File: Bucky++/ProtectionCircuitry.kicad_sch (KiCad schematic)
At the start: 0 parts

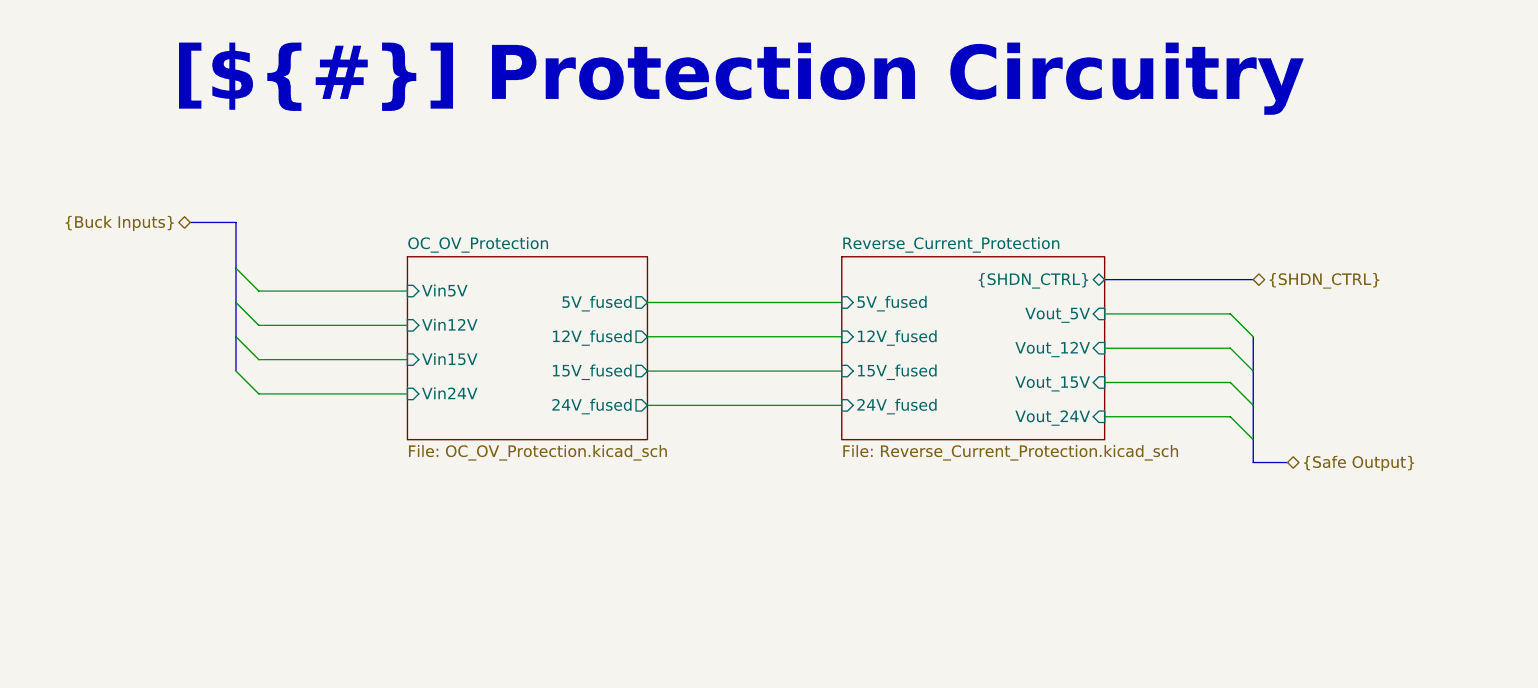
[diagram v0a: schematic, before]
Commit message: added over-current protection on main input
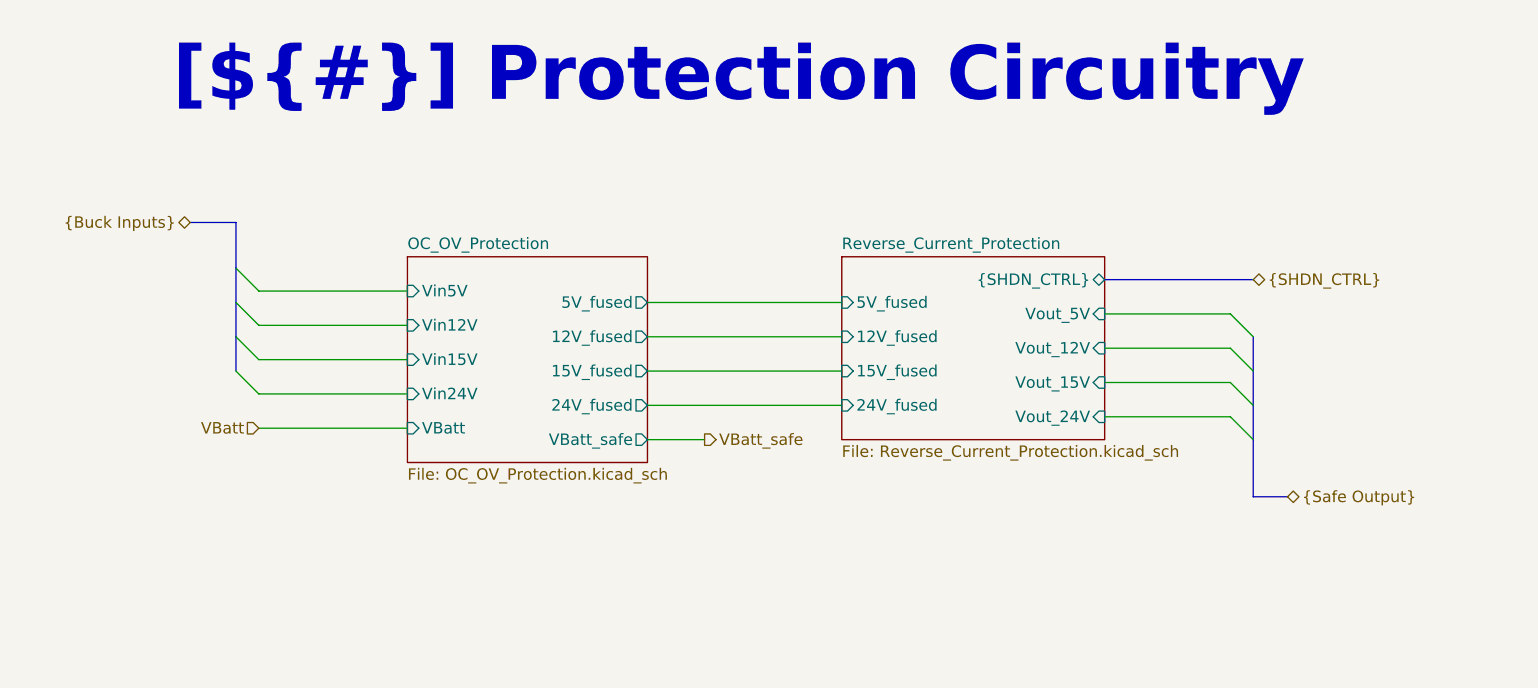
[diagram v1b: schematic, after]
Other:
- sheet OC_OV_Protection ports: added VBatt, VBatt_safe; removed none
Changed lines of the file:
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@@
+		)
+	)
+	(wire
+		(pts
+			(xy 144.78 59.69) (xy 158.75 59.69)
+		)
+		(stroke
+			(width 0)
+			(type default)
 		)
 	)
@@
 	(wire
 		(pts
+			(xy 50.8 60.96) (xy 67.31 60.96)
+		)
+		(stroke
+			(width 0)
+			(type default)
+		)
+	)
+	(wire
+		(pts
 			(xy 50.8 49.53) (xy 67.31 49.53)
 		)
@@
 	(bus
 		(pts
-			(xy 161.29 64.77) (xy 165.1 64.77)
+			(xy 161.29 68.58) (xy 165.1 68.58)
 		)
 		(stroke
@@
 	(wire
 		(pts
+			(xy 93.98 62.23) (xy 100.33 62.23)
+		)
+		(stroke
+			(width 0)
+			(type default)
+		)
+	)
+	(wire
+		(pts
 			(xy 93.98 58.42) (xy 115.57 58.42)
 		)
@@
 	(wire
 		(pts
-			(xy 144.78 59.69) (xy 158.75 59.69)
-		)
-		(stroke
-			(width 0)
-			(type default)
-		)
-	)
-	(wire
-		(pts
 			(xy 50.8 53.34) (xy 67.31 53.34)
 		)
@@
 	(bus
 		(pts
-			(xy 161.29 62.23) (xy 161.29 64.77)
+			(xy 161.29 62.23) (xy 161.29 68.58)
 		)
 		(stroke
@@
 	(hierarchical_label "{Safe Output}"
 		(shape tri_state)
-		(at 165.1 64.77 0)
+		(at 165.1 68.58 0)
 		(effects
 			(font
@@
 			)
 			(justify left)
+		)
+	)
+	(hierarchical_label "VBatt_safe"
+		(shape output)
+		(at 100.33 62.23 0)
+		(effects
+			(font
+				(size 1.27 1.27)
+			)
+			(justify left)
+		)
+	)
+	(hierarchical_label "VBatt"
+		(shape input)
+		(at 50.8 60.96 180)
+		(effects
+			(font
+				(size 1.27 1.27)
+			)
+			(justify right)
 		)
 	)
 	(sheet
 		(at 67.31 41.91)
-		(size 26.67 20.32)
+		(size 26.67 22.86)
 		(exclude_from_sim no)
 		(in_bom yes)
@@
 		)
 		(property "Sheetfile" "OC_OV_Protection.kicad_sch"
-			(at 67.31 62.8146 0)
+			(at 67.31 65.3546 0)
 			(effects
 				(font
@@
 			)
 		)
+		(pin "VBatt" input
+			(at 67.31 60.96 180)
+			(effects
+				(font
+					(size 1.27 1.27)
+				)
+				(justify left)
+			)
+		)
+		(pin "VBatt_safe" output
+			(at 93.98 62.23 0)
+			(effects
+				(font
+					(size 1.27 1.27)
+				)
+				(justify right)
+			)
+		)

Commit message: fixed errors and added protection diodes
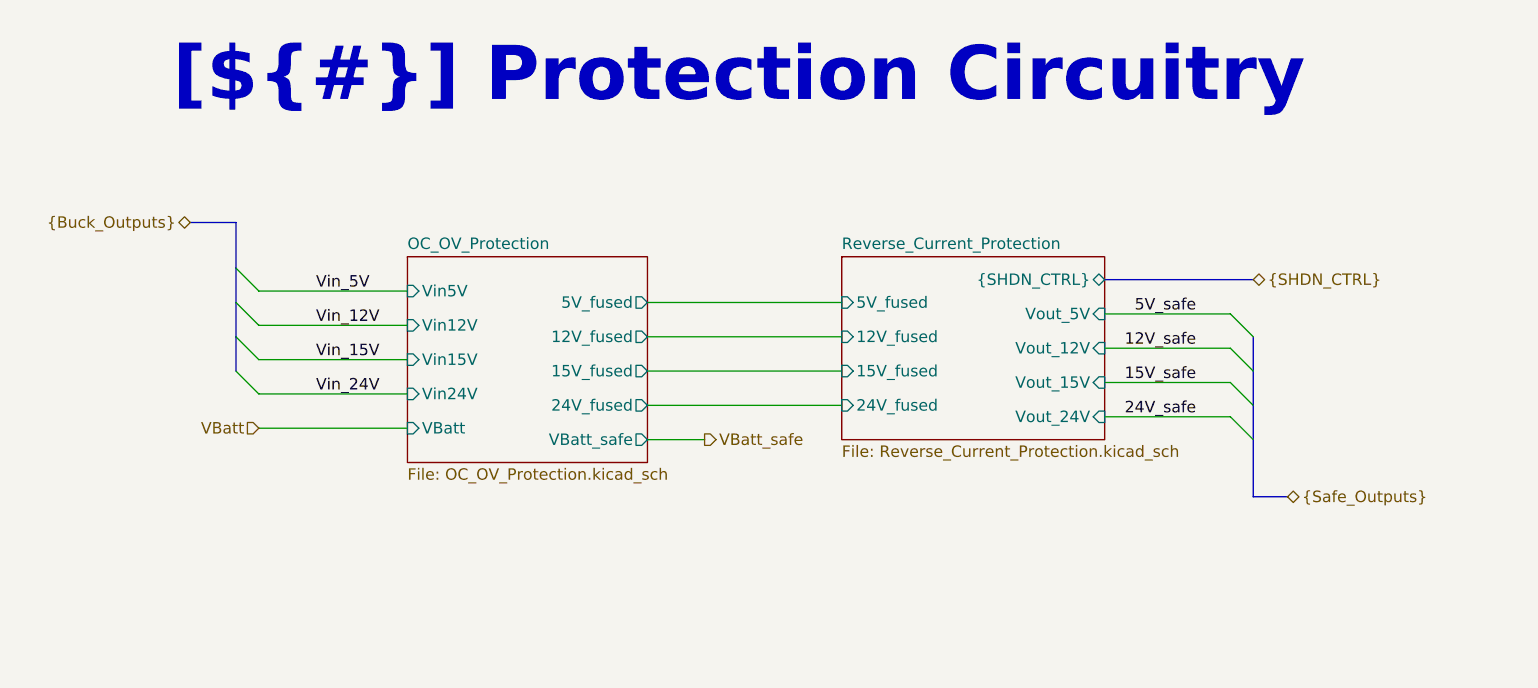
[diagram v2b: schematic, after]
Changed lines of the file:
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@@
+		)
+	)
+	(label "Vin_5V"
+		(at 57.15 45.72 0)
+		(effects
+			(font
+				(size 1.27 1.27)
+			)
+			(justify left bottom)
+		)
+	)
+	(label "Vin_15V"
+		(at 57.15 53.34 0)
+		(effects
+			(font
+				(size 1.27 1.27)
+			)
+			(justify left bottom)
+		)
+	)
+	(label "5V_safe"
+		(at 154.94 48.26 180)
+		(effects
+			(font
+				(size 1.27 1.27)
+			)
+			(justify right bottom)
+		)
+	)
+	(label "24V_safe"
+		(at 154.94 59.69 180)
+		(effects
+			(font
+				(size 1.27 1.27)
+			)
+			(justify right bottom)
+		)
+	)
+	(label "Vin_24V"
+		(at 57.15 57.15 0)
+		(effects
+			(font
+				(size 1.27 1.27)
+			)
+			(justify left bottom)
+		)
+	)
+	(label "Vin_12V"
+		(at 57.15 49.53 0)
+		(effects
+			(font
+				(size 1.27 1.27)
+			)
+			(justify left bottom)
+		)
+	)
+	(label "12V_safe"
+		(at 154.94 52.07 180)
+		(effects
+			(font
+				(size 1.27 1.27)
+			)
+			(justify right bottom)
+		)
+	)
+	(label "15V_safe"
+		(at 154.94 55.88 180)
+		(effects
+			(font
+				(size 1.27 1.27)
+			)
+			(justify right bottom)
 		)
 	)
@@
 		)
 	)
-	(hierarchical_label "{Buck Inputs}"
+	(hierarchical_label "{Buck_Outputs}"
 		(shape tri_state)
 		(at 43.18 38.1 180)
@@
 		)
 	)
-	(hierarchical_label "{Safe Output}"
+	(hierarchical_label "{Safe_Outputs}"
 		(shape tri_state)
 		(at 165.1 68.58 0)

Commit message: worked on layout, added adm1270
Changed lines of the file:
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@@
-	)
-	(bus_entry
-		(at 48.26 43.18)
-		(size 2.54 2.54)
-		(stroke
-			(width 0)
-			(type default)
-		)
 	)
 	(bus_entry
@@
 	)
 	(bus_entry
-		(at 48.26 50.8)
-		(size 2.54 2.54)
-		(stroke
-			(width 0)
-			(type default)
-		)
-	)
-	(bus_entry
-		(at 48.26 46.99)
+		(at 53.34 43.18)
 		(size 2.54 2.54)
 		(stroke
@@
 	)
 	(bus_entry
-		(at 48.26 54.61)
-		(size 2.54 2.54)
-		(stroke
-			(width 0)
-			(type default)
-		)
-	)
-	(wire
-		(pts
-			(xy 50.8 57.15) (xy 67.31 57.15)
-		)
+		(at 53.34 54.61)
+		(size 2.54 2.54)
+		(stroke
+			(width 0)
+			(type default)
+		)
+	)
+	(bus_entry
+		(at 53.34 46.99)
+		(size 2.54 2.54)
+		(stroke
+			(width 0)
+			(type default)
+		)
+	)
+	(bus_entry
+		(at 53.34 50.8)
+		(size 2.54 2.54)
 		(stroke
 			(width 0)
@@
 		)
 	)
-	(bus
-		(pts
-			(xy 48.26 46.99) (xy 48.26 50.8)
-		)
-		(stroke
-			(width 0)
-			(type default)
-		)
-	)
 	(wire
 		(pts
@@
 		)
 	)
-	(bus
-		(pts
-			(xy 48.26 43.18) (xy 48.26 46.99)
+	(wire
+		(pts
+			(xy 176.53 52.07) (xy 179.07 52.07)
 		)
 		(stroke
@@
 	(wire
 		(pts
-			(xy 50.8 49.53) (xy 67.31 49.53)
+			(xy 55.88 45.72) (xy 67.31 45.72)
+		)
+		(stroke
+			(width 0)
+			(type default)
+		)
+	)
+	(bus
+		(pts
+			(xy 53.34 43.18) (xy 53.34 38.1)
 		)
 		(stroke
@@
 		)
 	)
+	(bus
+		(pts
+			(xy 53.34 54.61) (xy 53.34 50.8)
+		)
+		(stroke
+			(width 0)
+			(type default)
+		)
+	)
+	(wire
+		(pts
+			(xy 55.88 49.53) (xy 67.31 49.53)
+		)
+		(stroke
+			(width 0)
+			(type default)
+		)
+	)
 	(wire
 		(pts
@@
 		)
 	)
+	(bus
+		(pts
+			(xy 53.34 38.1) (xy 45.72 38.1)
+		)
+		(stroke
+			(width 0)
+			(type default)
+		)
+	)
 	(wire
 		(pts
@@
 	(bus
 		(pts
-			(xy 43.18 38.1) (xy 48.26 38.1)
-		)
-		(stroke
-			(width 0)
-			(type default)
-		)
-	)
-	(bus
-		(pts
-			(xy 48.26 50.8) (xy 48.26 54.61)
+			(xy 53.34 46.99) (xy 53.34 43.18)
 		)
 		(stroke
@@
 		)
 	)
+	(wire
+		(pts
+			(xy 55.88 53.34) (xy 67.31 53.34)
+		)
+		(stroke
+			(width 0)
+			(type default)
+		)
+	)
+	(wire
+		(pts
+			(xy 55.88 57.15) (xy 67.31 57.15)
+		)
+		(stroke
+			(width 0)
+			(type default)
+		)
+	)
 	(bus
 		(pts
@@
 	(bus
 		(pts
-			(xy 48.26 38.1) (xy 48.26 43.18)
-		)
-		(stroke
-			(width 0)
-			(type default)
-		)
-	)
-	(wire
-		(pts
-			(xy 50.8 53.34) (xy 67.31 53.34)
+			(xy 53.34 50.8) (xy 53.34 46.99)
 		)
 		(stroke
@@
 		)
 	)
-	(wire
-		(pts
-			(xy 50.8 45.72) (xy 67.31 45.72)
-		)
-		(stroke
-			(width 0)
-			(type default)
-		)
-	)
 	(bus
 		(pts
@@
 		)
 	)
-	(label "Vin_5V"
-		(at 57.15 45.72 0)
-		(effects
-			(font
-				(size 1.27 1.27)
-			)
-			(justify left bottom)
-		)
-	)
-	(label "Vin_15V"
-		(at 57.15 53.34 0)
-		(effects
-			(font
-				(size 1.27 1.27)
-			)
-			(justify left bottom)
+	(label "12V_safe"
+		(at 176.53 52.07 180)
+		(effects
+			(font
+				(size 1.27 1.27)
+			)
+			(justify right bottom)
 		)
 	)
@@
 		)
 	)
+	(label "out24V"
+		(at 67.31 57.15 180)
+		(effects
+			(font
+				(size 1.27 1.27)
+			)
+			(justify right bottom)
+		)
+	)
 	(label "24V_safe"
 		(at 154.94 59.69 180)
@@
 		)
 	)
-	(label "Vin_24V"
-		(at 57.15 57.15 0)
-		(effects
-			(font
-				(size 1.27 1.27)
-			)
-			(justify left bottom)
-		)
-	)
-	(label "Vin_12V"
-		(at 57.15 49.53 0)
-		(effects
-			(font
-				(size 1.27 1.27)
-			)
-			(justify left bottom)
-		)
-	)
 	(label "12V_safe"
 		(at 154.94 52.07 180)
@@
 		)
 	)
+	(label "out12V"
+		(at 67.31 49.53 180)
+		(effects
+			(font
+				(size 1.27 1.27)
+			)
+			(justify right bottom)
+		)
+	)
+	(label "out5V"
+		(at 67.31 45.72 180)
+		(effects
+			(font
+				(size 1.27 1.27)
+			)
+			(justify right bottom)
+		)
+	)
 	(label "15V_safe"
 		(at 154.94 55.88 180)
+		(effects
+			(font
+				(size 1.27 1.27)
+			)
+			(justify right bottom)
+		)
+	)
+	(label "out15V"
+		(at 67.31 53.34 180)
 		(effects
 			(font
@@
 		)
 	)
-	(hierarchical_label "{Buck_Outputs}"
+	(hierarchical_label "{Shunt_Outputs}"
 		(shape tri_state)
-		(at 43.18 38.1 180)
+		(at 45.72 38.1 180)
 		(effects
 			(font
@@
 		)
 	)
-	(hierarchical_label "VBatt"
+	(hierarchical_label "12V_fans"
+		(shape output)
+		(at 179.07 52.07 0)
+		(effects
+			(font
+				(size 1.27 1.27)
+			)
+			(justify left)
+		)
+	)
+	(hierarchical_label "VBatt_protection"
 		(shape input)
 		(at 50.8 60.96 180)

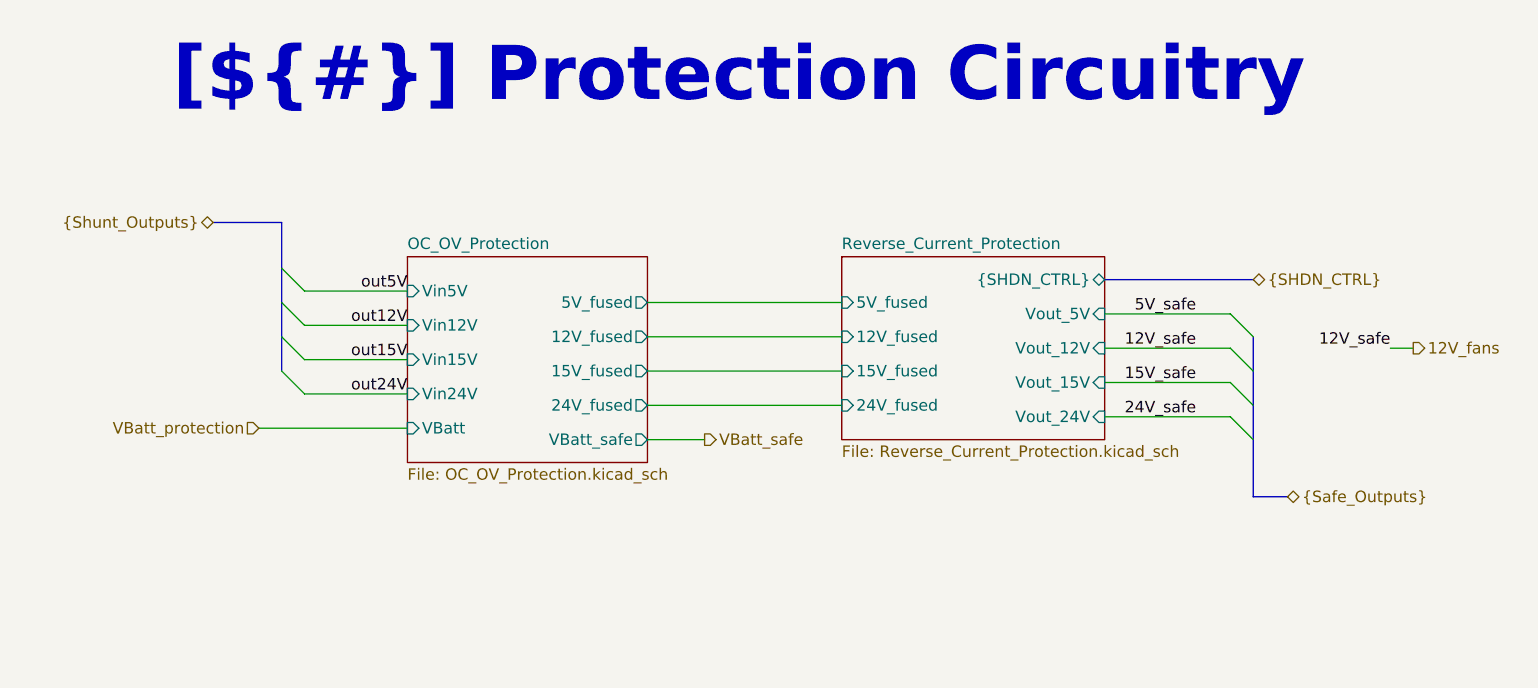
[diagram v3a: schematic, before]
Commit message: updated circuit after review. updated silkscreen
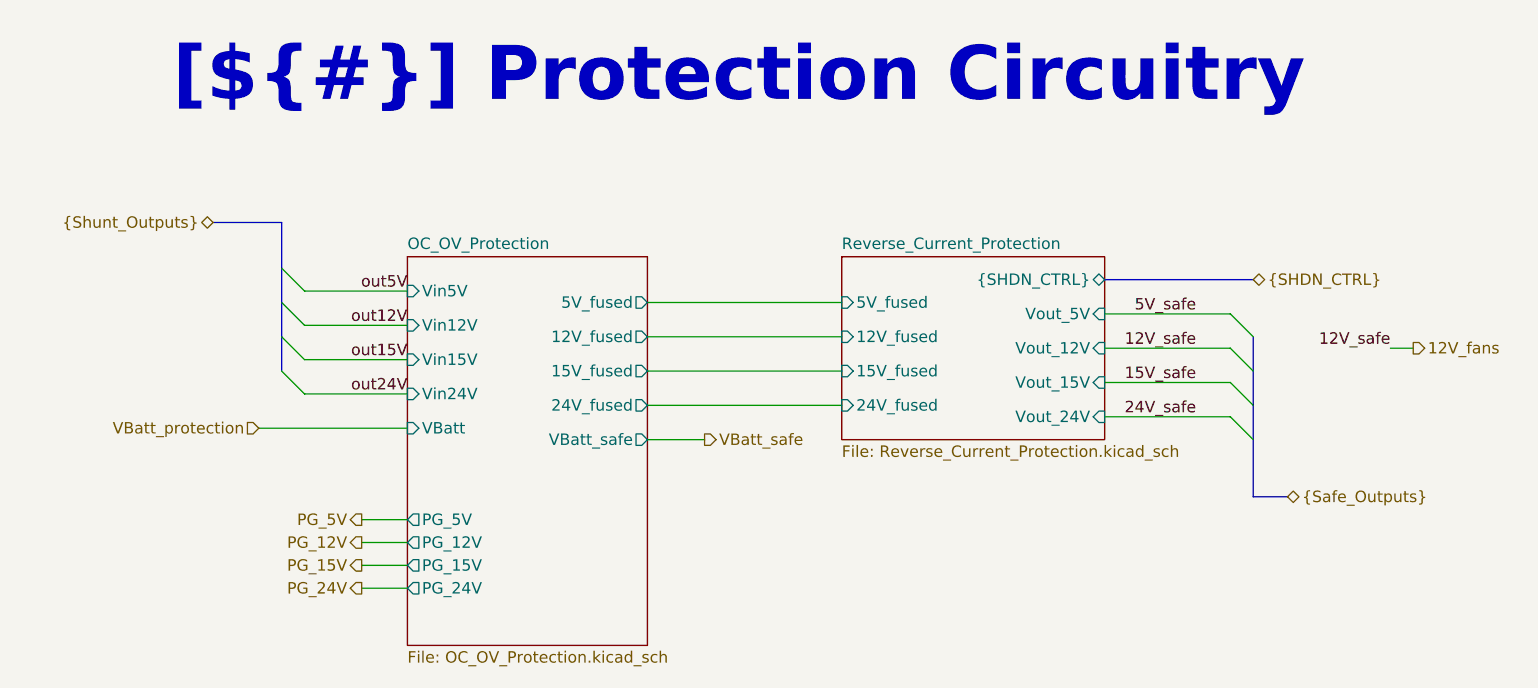
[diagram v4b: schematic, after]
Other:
- sheet OC_OV_Protection ports: added PG_12V, PG_15V, PG_24V, PG_5V; removed none
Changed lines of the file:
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@@
+	(wire
+		(pts
+			(xy 62.23 78.74) (xy 67.31 78.74)
+		)
+		(stroke
+			(width 0)
+			(type default)
+		)
+	)
 	(wire
 		(pts
@@
 	(wire
 		(pts
+			(xy 62.23 76.2) (xy 67.31 76.2)
+		)
+		(stroke
+			(width 0)
+			(type default)
+		)
+	)
+	(wire
+		(pts
 			(xy 93.98 58.42) (xy 115.57 58.42)
 		)
@@
 	(wire
 		(pts
+			(xy 62.23 71.12) (xy 67.31 71.12)
+		)
+		(stroke
+			(width 0)
+			(type default)
+		)
+	)
+	(wire
+		(pts
 			(xy 55.88 57.15) (xy 67.31 57.15)
 		)
@@
 		(pts
 			(xy 53.34 50.8) (xy 53.34 46.99)
+		)
+		(stroke
+			(width 0)
+			(type default)
+		)
+	)
+	(wire
+		(pts
+			(xy 62.23 73.66) (xy 67.31 73.66)
 		)
 		(stroke
@@
 		)
 	)
+	(hierarchical_label "PG_15V"
+		(shape output)
+		(at 62.23 76.2 180)
+		(effects
+			(font
+				(size 1.27 1.27)
+			)
+			(justify right)
+		)
+	)
 	(hierarchical_label "VBatt_protection"
 		(shape input)
@@
 		)
 	)
+	(hierarchical_label "PG_5V"
+		(shape output)
+		(at 62.23 71.12 180)
+		(effects
+			(font
+				(size 1.27 1.27)
+			)
+			(justify right)
+		)
+	)
+	(hierarchical_label "PG_24V"
+		(shape output)
+		(at 62.23 78.74 180)
+		(effects
+			(font
+				(size 1.27 1.27)
+			)
+			(justify right)
+		)
+	)
+	(hierarchical_label "PG_12V"
+		(shape output)
+		(at 62.23 73.66 180)
+		(effects
+			(font
+				(size 1.27 1.27)
+			)
+			(justify right)
+		)
+	)
 	(sheet
 		(at 67.31 41.91)
-		(size 26.67 22.86)
+		(size 26.67 43.18)
 		(exclude_from_sim no)
 		(in_bom yes)
@@
 		)
 		(property "Sheetfile" "OC_OV_Protection.kicad_sch"
-			(at 67.31 65.3546 0)
+			(at 67.31 85.6746 0)
 			(effects
 				(font
@@
 			)
 		)
+		(pin "PG_5V" output
+			(at 67.31 71.12 180)
+			(effects
+				(font
+					(size 1.27 1.27)
+				)
+				(justify left)
+			)
+		)
+		(pin "PG_15V" output
+			(at 67.31 76.2 180)
+			(effects
+				(font
+					(size 1.27 1.27)
+				)
+				(justify left)
+			)
+		)
+		(pin "PG_24V" output
+			(at 67.31 78.74 180)
+			(effects
+				(font
+					(size 1.27 1.27)
+				)
+				(justify left)
+			)
+		)
+		(pin "PG_12V" output
+			(at 67.31 73.66 180)
+			(effects
+				(font
+					(size 1.27 1.27)
+				)
+				(justify left)
+			)
+		)

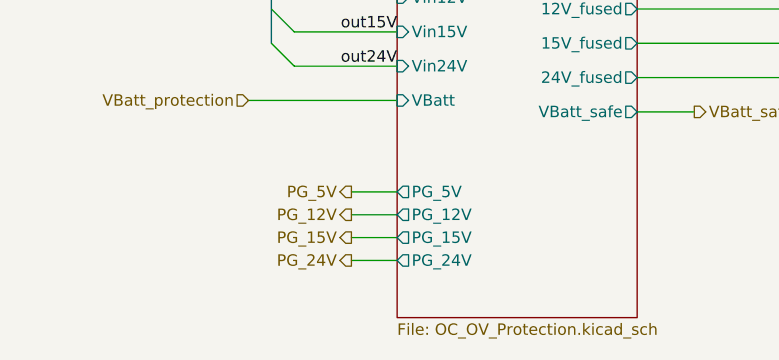
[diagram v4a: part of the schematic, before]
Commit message: fix layout and tolerance issues, started working on routing alerts
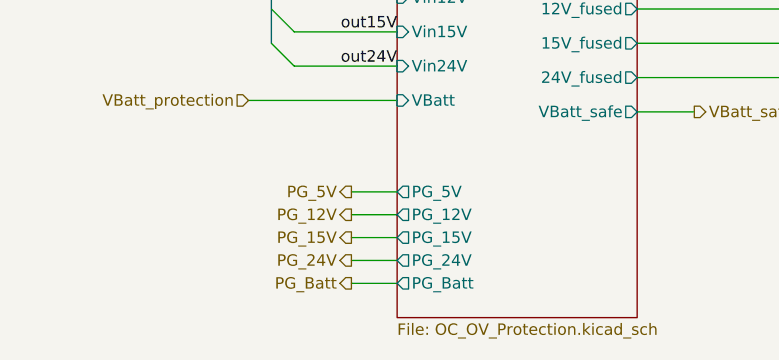
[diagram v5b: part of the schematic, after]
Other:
- sheet OC_OV_Protection ports: added PG_Batt; removed none
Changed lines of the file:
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@@
+	(wire
+		(pts
+			(xy 62.23 81.28) (xy 67.31 81.28)
+		)
+		(stroke
+			(width 0)
+			(type default)
+		)
+	)
 	(wire
 		(pts
@@
 		(shape tri_state)
 		(at 45.72 38.1 180)
+		(effects
+			(font
+				(size 1.27 1.27)
+			)
+			(justify right)
+		)
+	)
+	(hierarchical_label "PG_Batt"
+		(shape output)
+		(at 62.23 81.28 180)
 		(effects
 			(font
@@
 			(effects
 				(font
+					(size 1.27 1.27)
+				)
+				(justify left)
+			)
+		)
+		(pin "PG_Batt" output
+			(at 67.31 81.28 180)
+			(effects
+				(font
